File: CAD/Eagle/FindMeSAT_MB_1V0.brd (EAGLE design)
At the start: 99 x 49.2 mm, 127 parts, among them IC1111 LM2831YMF, J291 MCX-J-P-X-RA-SM1, J681 SMA_CON, J701 MOLEX_105017-0001, J801 MICROSIM-8P_SDCARD-8P_MOLEX-1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, J901 JST_S3B-XH-A, Q101 ABS07, Q651 ABM3B-16MHZ-10-R50-1-U, U1001 CFPT-141, U101 ATXMEGA256A3BU-AU, U1011 OPA354, U1021 OPA354, U1121 LM4120IM5-3.0, U201 SIM808, U301 9DoF IMU, U401 BMP180, U501 SHT31-DIS, U601 AX5243

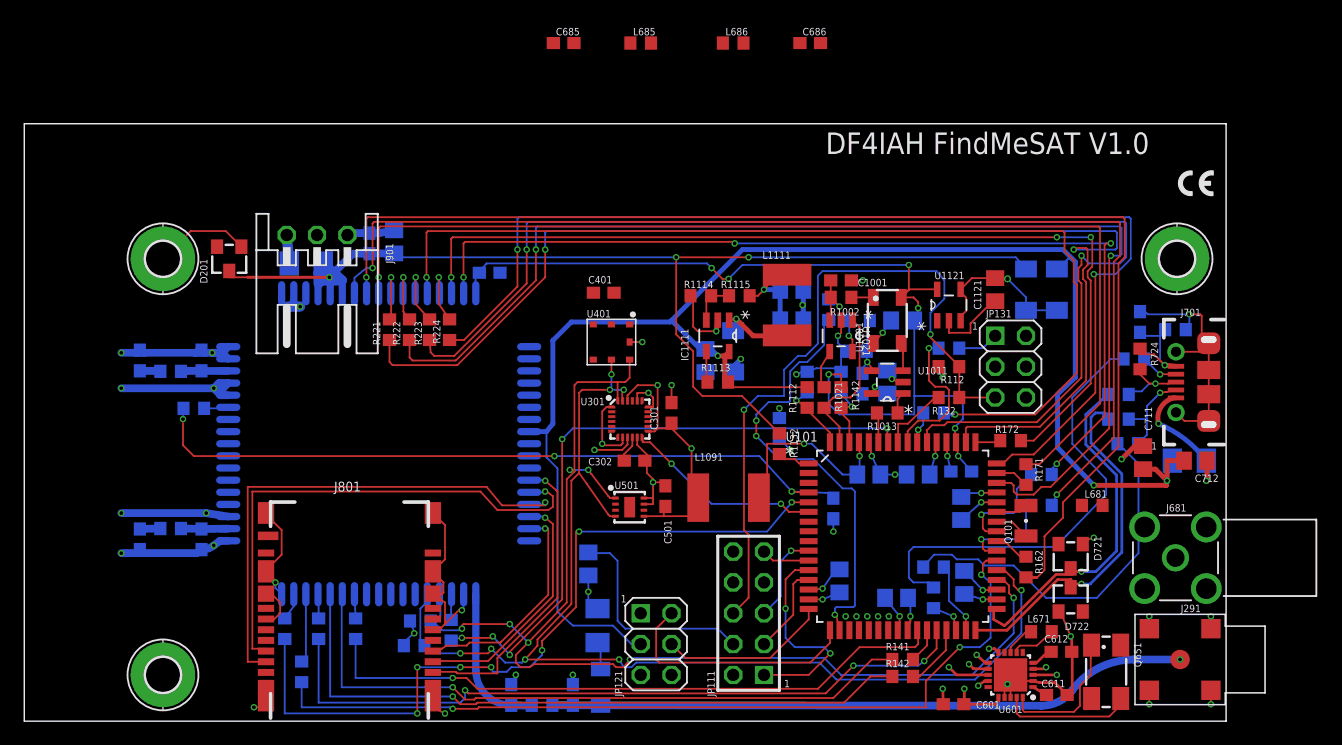
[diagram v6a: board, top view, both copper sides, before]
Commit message: Eagle - more fine tuning after CPU block movement done
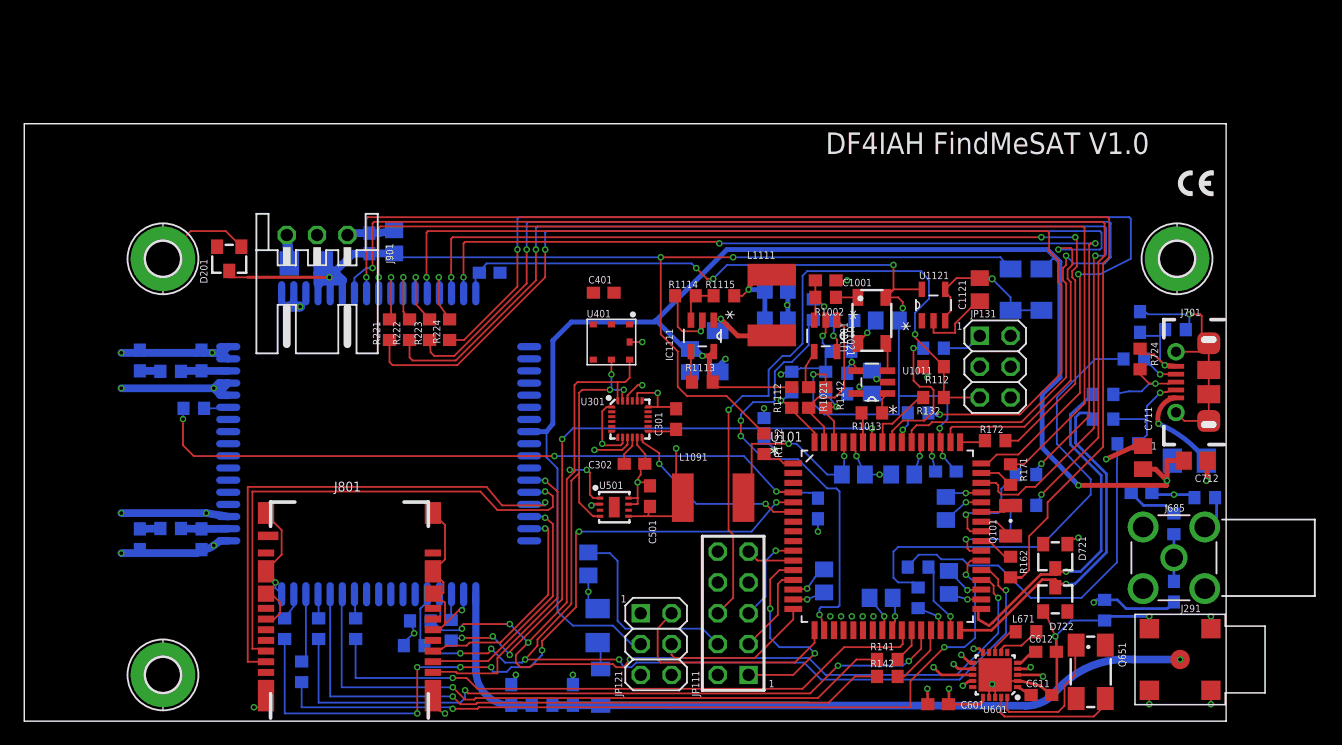
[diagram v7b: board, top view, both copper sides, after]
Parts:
- removed C685: 22p, rcl:C0603
- removed J681: SMA_CON, df4iah_connector:SMA_SMT_AMPHENOL_901-143
- removed L685: 82nH, rcl:R0603
- added C681: 68p, rcl:C0603
- added J685: SMA_CON, df4iah_connector:SMA_SMT_AMPHENOL_901-143
- added L682: 68nH, rcl:R0603
- C686: value 15p -> 18p
- L686: value 82nH -> 150nH
- moved L686 55.9 mm to (89.0, 9.14), flipped to the bottom, turned to 90 degrees
- moved C686 54.2 mm to (94.7, 10.7), flipped to the bottom, turned to 90 degrees
- moved L681 9.29 mm to (97.3, 18.4), flipped to the bottom, turned to 180 degrees
- moved C1012 1.27 mm to (69.8, 27.9)
- moved C1091 1.27 mm to (65.9, 11.6)
- moved C1092 1.27 mm to (70.6, 10.2)
- moved C1096 1.27 mm to (68.3, 20.3)
- moved C1121 1.27 mm to (78.7, 35.6)
- moved C611 1.27 mm to (83.8, 2.16)
- moved C612 1.27 mm to (84.2, 5.71)
- moved D1121 1.27 mm to (83.8, 35.6)
- moved D721 1.27 mm to (85.0, 13.6)
- moved D722 1.27 mm to (85.0, 10.0)
- moved R1012 1.27 mm to (67.6, 33.0)
- moved R1013 1.27 mm to (69.8, 25.4)
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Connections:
- new net AX_ANT_I: C681.2, L682.1
- net AX_ANT: now also J685.1, L682.2; no longer J681.1, L686.2
- net AX_ANTN: now also L686.2; no longer L685.2
- net AX_ANTP: now also C681.1; no longer C685.2, L686.1
- net GND: now also J685.2, J685.3, J685.4, J685.5, L686.1; no longer C685.1, J681.2, J681.3, J681.4, J681.5, L685.1
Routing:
- net AX_ANTP: track 1.96 -> 25.7 mm, vias 1 -> 2
- net AX_ANTN: track 1.13 -> 17.0 mm, vias 1 -> 2
- net GND: track 200.2 -> 214.5 mm
- net +3V3: track 65.3 -> 58.0 mm
- net AX_ANT_I: track 0.00 -> 4.22 mm
- net AX_ANT: track 0.00 -> 3.89 mm
- net SDA1: track 99.2 -> 97.6 mm
- net SCL1: track 100.3 -> 98.8 mm
- net SCL2: track 20.5 -> 19.0 mm
- net DTR1: track 97.0 -> 95.7 mm
- net RTS1: track 98.7 -> 97.4 mm
- net RI1: track 98.5 -> 97.2 mm
- net GSM_PCM_IN: track 56.0 -> 54.7 mm
- net GSM_PCM_CLK: track 54.9 -> 53.6 mm
- net +3V0: track 77.9 -> 76.7 mm
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
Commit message: Eagle - antennas for GSM and BT added
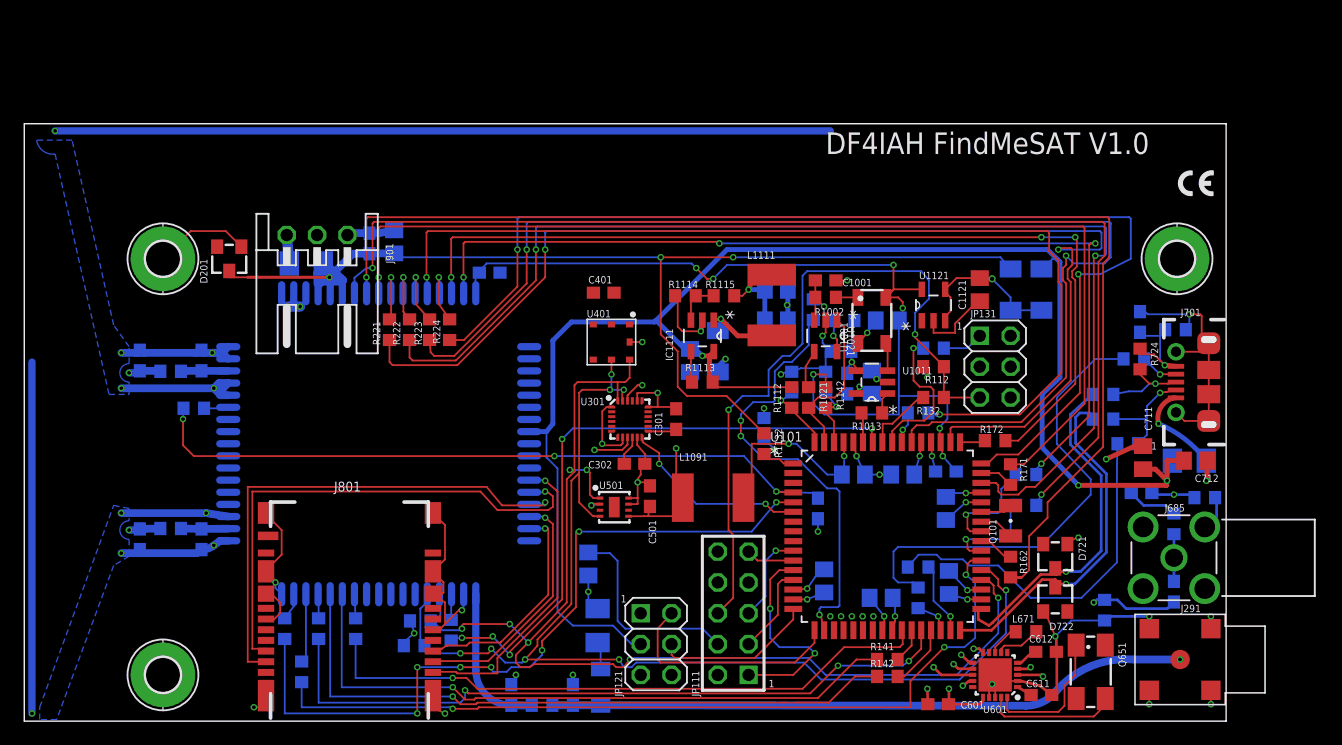
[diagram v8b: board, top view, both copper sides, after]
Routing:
- net GSM_ANT: track 1.87 -> 88.3 mm, vias 0 -> 2
- net BT_ANT: track 1.69 -> 49.8 mm, vias 0 -> 2
- added copper zone on layer 16, net GND
- added copper zone on layer 2, net GND
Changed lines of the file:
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@@
 <grid distance="1.27" unitdist="mm" unit="mm" style="lines" multiple="1" display="yes" altdistance="0.127" altunitdist="mm" altunit="mm"/>
 <layers>
-<layer number="1" name="Top" color="4" fill="1" visible="yes" active="yes"/>
+<layer number="1" name="Top" color="4" fill="1" visible="no" active="yes"/>
 <layer number="2" name="Route2" color="1" fill="3" visible="yes" active="yes"/>
 <layer number="3" name="Route3" color="4" fill="3" visible="no" active="no"/>
 <layer number="14" name="Route14" color="1" fill="6" visible="no" active="no"/>
-<layer number="15" name="Route15" color="4" fill="6" visible="yes" active="yes"/>
-<layer number="16" name="Bottom" color="1" fill="1" visible="yes" active="yes"/>
+<layer number="15" name="Route15" color="4" fill="6" visible="no" active="yes"/>
+<layer number="16" name="Bottom" color="1" fill="1" visible="no" active="yes"/>
 <layer number="17" name="Pads" color="2" fill="1" visible="yes" active="yes"/>
 <layer number="18" name="Vias" color="2" fill="1" visible="yes" active="yes"/>
@@
 <layer number="23" name="tOrigins" color="15" fill="1" visible="yes" active="yes"/>
 <layer number="24" name="bOrigins" color="15" fill="1" visible="yes" active="yes"/>
-<layer number="25" name="tNames" color="7" fill="1" visible="yes" active="yes"/>
+<layer number="25" name="tNames" color="7" fill="1" visible="no" active="yes"/>
 <layer number="26" name="bNames" color="7" fill="1" visible="no" active="yes"/>
 <layer number="27" name="tValues" color="7" fill="1" visible="no" active="yes"/>
@@
 <layer number="37" name="tTest" color="7" fill="1" visible="no" active="yes"/>
 <layer number="38" name="bTest" color="7" fill="1" visible="no" active="yes"/>
-<layer number="39" name="tKeepout" color="4" fill="11" visible="yes" active="yes"/>
-<layer number="40" name="bKeepout" color="1" fill="11" visible="yes" active="yes"/>
+<layer number="39" name="tKeepout" color="4" fill="11" visible="no" active="yes"/>
+<layer number="40" name="bKeepout" color="1" fill="11" visible="no" active="yes"/>
 <layer number="41" name="tRestrict" color="4" fill="10" visible="yes" active="yes"/>
 <layer number="42" name="bRestrict" color="1" fill="10" visible="yes" active="yes"/>
 <layer number="43" name="vRestrict" color="2" fill="10" visible="yes" active="yes"/>
-<layer number="44" name="Drills" color="7" fill="1" visible="no" active="yes"/>
-<layer number="45" name="Holes" color="7" fill="1" visible="no" active="yes"/>
-<layer number="46" name="Milling" color="3" fill="1" visible="no" active="yes"/>
-<layer number="47" name="Measures" color="7" fill="1" visible="no" active="yes"/>
+<layer number="44" name="Drills" color="7" fill="1" visible="yes" active="yes"/>
+<layer number="45" name="Holes" color="7" fill="1" visible="yes" active="yes"/>
+<layer number="46" name="Milling" color="3" fill="1" visible="yes" active="yes"/>
+<layer number="47" name="Measures" color="7" fill="1" visible="yes" active="yes"/>
 <layer number="48" name="Document" color="7" fill="1" visible="no" active="yes"/>
-<layer number="49" name="Reference" color="7" fill="1" visible="no" active="yes"/>
+<layer number="49" name="Reference" color="7" fill="1" visible="yes" active="yes"/>
 <layer number="50" name="dxf" color="7" fill="1" visible="no" active="no"/>
-<layer number="51" name="tDocu" color="7" fill="1" visible="no" active="yes"/>
-<layer number="52" name="bDocu" color="7" fill="1" visible="no" active="yes"/>
+<layer number="51" name="tDocu" color="7" fill="1" visible="yes" active="yes"/>
+<layer number="52" name="bDocu" color="7" fill="1" visible="yes" active="yes"/>
 <layer number="53" name="tGND_GNDA" color="7" fill="9" visible="no" active="no"/>
 <layer number="54" name="bGND_GNDA" color="1" fill="9" visible="no" active="no"/>
@@
 </polygon>
 <text x="49.149" y="9.779" size="0.6096" layer="21" ratio="20">1</text>
+<dimension x1="2.54" y1="48.641" x2="66.675" y2="48.641" x3="34.6075" y3="50.292" textsize="0.6096" layer="47"/>
+<dimension x1="0.635" y1="0.635" x2="0.635" y2="29.845" x3="-1.016" y3="15.24" textsize="0.6096" layer="47"/>
 </plain>
 <attributes>
@@
 <wire x1="89.535" y1="8.636" x2="89.193" y2="8.128" width="0.225" layer="16"/>
 <wire x1="89.193" y1="8.128" x2="89.027" y2="8.294" width="0.225" layer="16"/>
+<wire x1="98.259" y1="16.852" x2="98.259" y2="18.288" width="0.225" layer="16"/>
+<wire x1="98.259" y1="18.288" x2="98.132" y2="18.415" width="0.225" layer="16"/>
+<polygon width="0.1" layer="16" thermals="no">
+<vertex x="8.636" y="16.51" curve="180"/>
+<vertex x="8.636" y="14.986"/>
+<vertex x="8.636" y="13.589"/>
+<vertex x="7.366" y="12.827"/>
+<vertex x="2.667" y="0.127"/>
+<vertex x="1.27" y="0.127"/>
+<vertex x="1.27" y="1.143"/>
+<vertex x="7.366" y="17.78"/>
+<vertex x="8.636" y="17.526"/>
+</polygon>
+<polygon width="0.1" layer="16" thermals="no">
+<vertex x="8.636" y="27.94" curve="-180"/>
+<vertex x="8.636" y="29.464"/>
+<vertex x="8.636" y="30.861"/>
+<vertex x="7.366" y="32.639"/>
+<vertex x="3.937" y="47.879"/>
+<vertex x="1.016" y="47.879" curve="90"/>
+<vertex x="2.54" y="46.736"/>
+<vertex x="6.985" y="26.924"/>
+<vertex x="8.636" y="26.924"/>
+</polygon>
 <wire x1="94.019" y1="32.258" x2="94.996" y2="38.1" width="0" layer="19" extent="16-16"/>
 <wire x1="92.202" y1="22.667" x2="93.98" y2="29.337" width="0" layer="19" extent="1-16"/>
 <wire x1="97.47" y1="21.463" x2="92.202" y2="22.667" width="0" layer="19" extent="1-1"/>
-<wire x1="98.259" y1="16.852" x2="97.47" y2="19.751" width="0" layer="19" extent="1-16"/>
+<wire x1="98.132" y1="18.415" x2="97.47" y2="19.751" width="0" layer="19" extent="1-16"/>
 <wire x1="92.202" y1="16.002" x2="97.282" y2="16.002" width="0" layer="19" extent="1-1"/>
 <wire x1="97.282" y1="10.922" x2="97.282" y2="16.002" width="0" layer="19" extent="1-1"/>
@@
 <wire x1="20.32" y1="2.104" x2="20.574" y2="8.382" width="0" layer="19" extent="1-1"/>
 <wire x1="11.43" y1="3.81" x2="18.923" y2="1.143" width="0" layer="19" extent="1-1"/>
-<wire x1="98.259" y1="16.852" x2="98.259" y2="18.288" width="0.225" layer="16"/>
-<wire x1="98.259" y1="18.288" x2="98.132" y2="18.415" width="0.225" layer="16"/>
+<polygon width="0.1" layer="2" thermals="no">
+<vertex x="8.636" y="16.51" curve="180"/>
+<vertex x="8.636" y="14.986"/>
+<vertex x="8.636" y="13.589"/>
+<vertex x="7.366" y="12.827"/>
+<vertex x="2.667" y="0.127"/>
+<vertex x="1.27" y="0.127"/>
+<vertex x="1.27" y="1.143"/>
+<vertex x="7.366" y="17.78"/>
+<vertex x="8.636" y="17.526"/>
+</polygon>
+<polygon width="0.1" layer="2" thermals="no">
+<vertex x="8.636" y="27.94" curve="-180"/>
+<vertex x="8.636" y="29.464"/>
+<vertex x="8.636" y="30.861"/>
+<vertex x="7.366" y="32.639"/>
+<vertex x="3.937" y="47.879"/>
+<vertex x="1.016" y="47.879" curve="90"/>
+<vertex x="2.54" y="46.736"/>
+<vertex x="6.985" y="26.924"/>
+<vertex x="8.636" y="26.924"/>
+</polygon>
 </signal>
 <signal name="EN">
@@
 <contactref element="C282" pad="1"/>
 <wire x1="11.215" y1="15.875" x2="9.525" y2="15.836" width="0.64" layer="16"/>
+<via x="8.636" y="15.748" extent="1-16" drill="0.3" shape="octagon"/>
+<wire x1="8.636" y1="15.748" x2="9.525" y2="15.748" width="0.604" layer="16"/>
+<wire x1="9.525" y1="15.748" x2="9.525" y2="15.836" width="0.604" layer="16"/>
+<wire x1="0.635" y1="29.591" x2="0.635" y2="0.635" width="0.604" layer="16"/>
+<via x="0.635" y="0.635" extent="1-16" drill="0.3" shape="octagon"/>
+<wire x1="0.635" y1="0.635" x2="1.397" y2="0.635" width="0.604" layer="15"/>
+<wire x1="1.397" y1="0.635" x2="2.159" y2="1.27" width="0.604" layer="15" curve="90"/>
+<wire x1="2.159" y1="1.27" x2="7.366" y2="15.367" width="0.604" layer="15"/>
+<wire x1="7.366" y1="15.367" x2="7.874" y2="15.748" width="0.604" layer="15" curve="-90"/>
+<wire x1="7.874" y1="15.748" x2="8.636" y2="15.748" width="0.604" layer="15"/>
 </signal>
 <signal name="GSM_RF" class="2">
@@
 <wire x1="11.215" y1="28.829" x2="11.303" y2="28.868" width="0.64" layer="16"/>
 <wire x1="11.303" y1="28.868" x2="9.525" y2="28.868" width="0.64" layer="16"/>
+<via x="8.636" y="28.702" extent="1-16" drill="0.3" shape="octagon"/>
+<wire x1="8.636" y1="28.702" x2="9.525" y2="28.702" width="0.604" layer="16"/>
+<wire x1="9.525" y1="28.702" x2="9.525" y2="28.868" width="0.604" layer="16"/>
+<via x="2.54" y="48.641" extent="1-16" drill="0.3" shape="octagon"/>
+<wire x1="8.636" y1="28.702" x2="8.128" y2="28.702" width="0.604" layer="15"/>
+<wire x1="8.128" y1="28.702" x2="7.239" y2="29.464" width="0.604" layer="15" curve="-90"/>
+<wire x1="7.239" y1="29.464" x2="3.302" y2="46.863" width="0.604" layer="15"/>
+<wire x1="3.302" y1="46.863" x2="2.794" y2="47.498" width="0.604" layer="15" curve="90"/>
+<wire x1="2.794" y1="47.498" x2="2.54" y2="48.641" width="0.604" layer="15" curve="-90"/>
+<wire x1="2.54" y1="48.641" x2="66.421" y2="48.641" width="0.604" layer="16"/>
 </signal>
 <signal name="GPS_PWR">
